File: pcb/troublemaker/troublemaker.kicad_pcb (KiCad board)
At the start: 2 copper layers, 419 x 394 mm, 116 parts, among them IC1 TEENSY_4.1, J1 neopixel_data_RPI19_GPIO10, J2 taptempo_led_RPI16_GPIO23, J3 5V_RPI2_OR_4, J4 GND_RPI34, J5 Conn_01x12, SW1 sw_eq2, SW10 sw_grain_playback, SW11 btn_sampler_stop, SW2 sw_eq1, SW3 sw_sub, SW4 sw_bass, SW5 sw_mid, SW6 sw_high, SW7 btn_delay_taptempo, SW8 sw_delay_type, SW9 sw_grain_type, U1 RASPBERRY_PI_4B_4GB, U2 CD74HC4067M, U3 CD74HC4067M, U4 CD74HC4067M, U5 CD74HC4067M, U6 CD74HC4067M

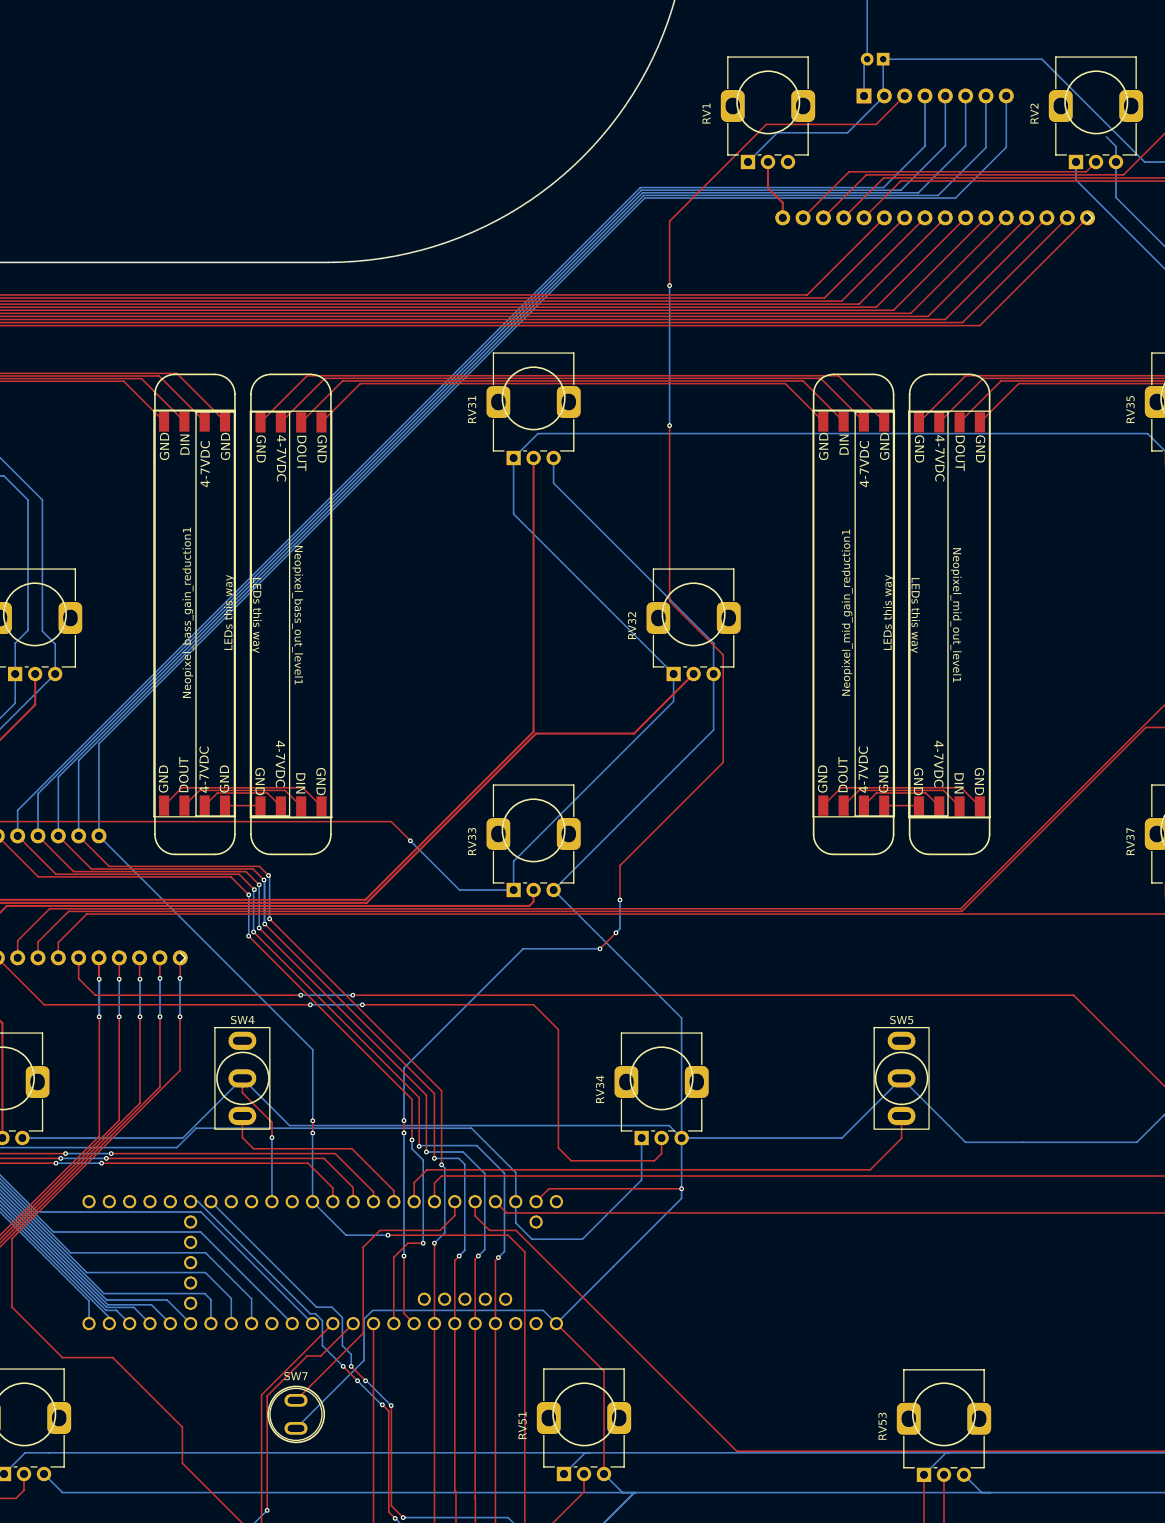
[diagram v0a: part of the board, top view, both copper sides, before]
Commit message: fixed missing connections
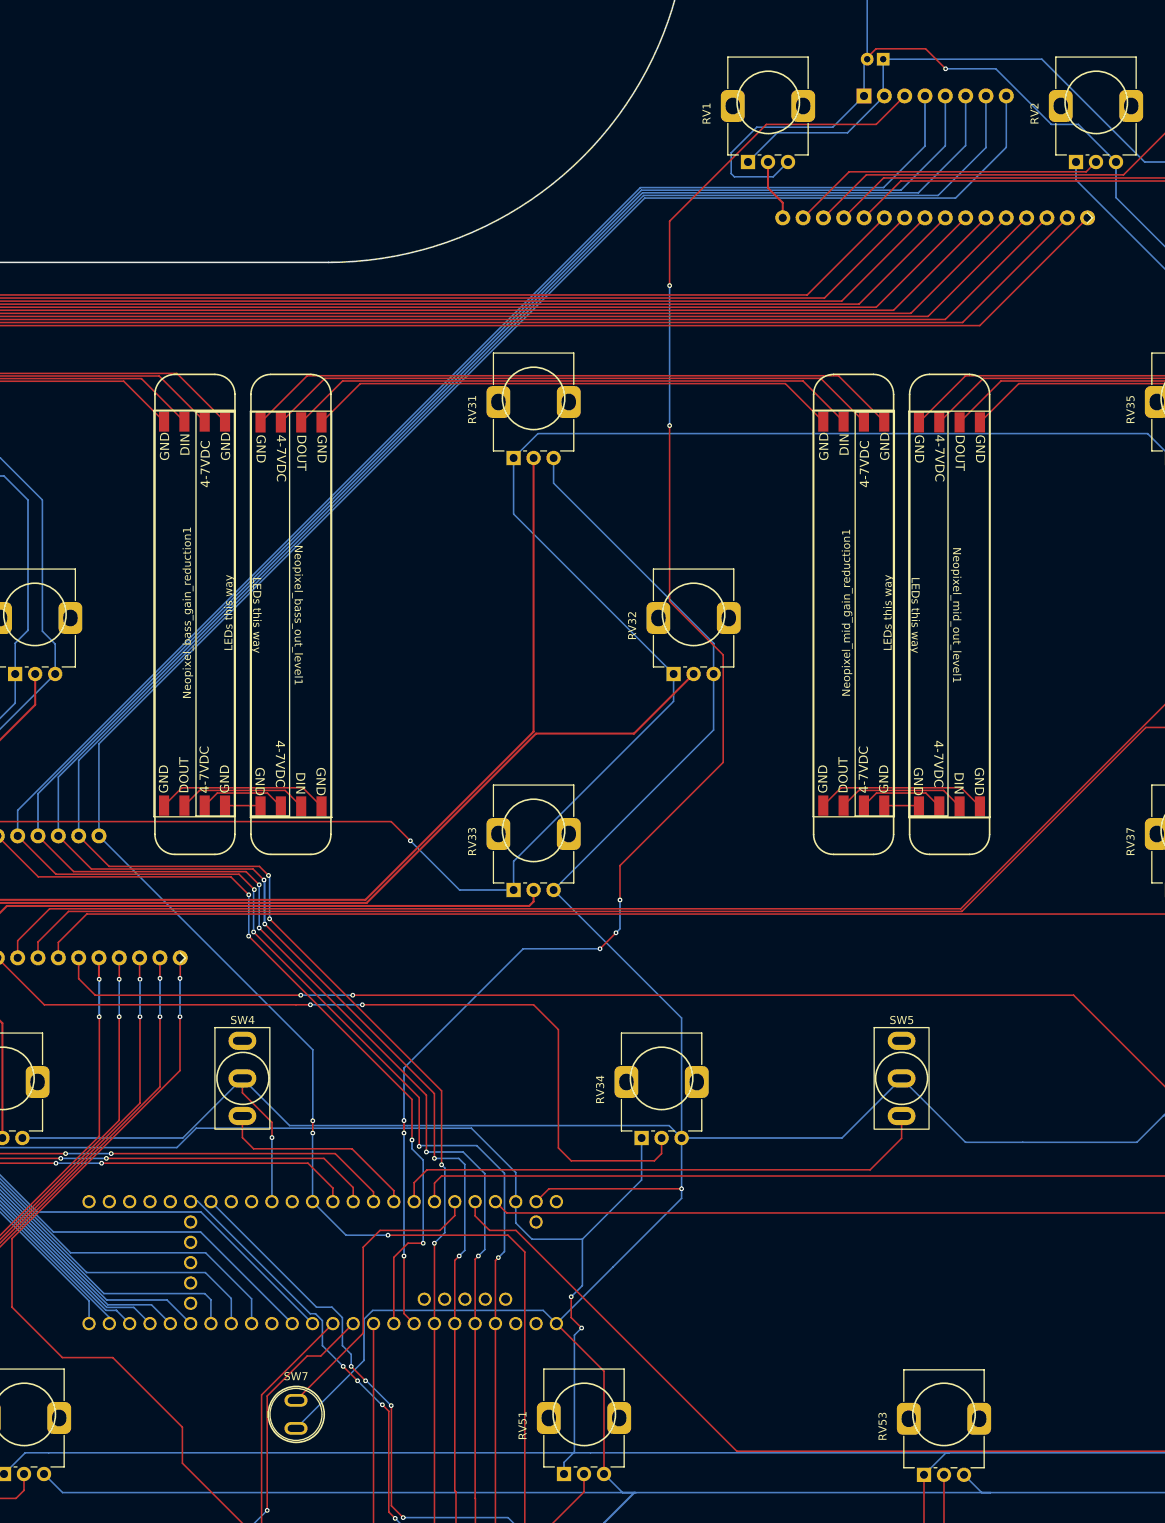
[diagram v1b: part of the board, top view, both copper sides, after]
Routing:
- net GND: track 3801.1 -> 3865.3 mm, vias 6 -> 7
- net 3v3: track 3703.4 -> 3730.4 mm, vias 8 -> 10
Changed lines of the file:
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@@
 	)
 	(segment
+		(start 314.9 209.6)
+		(end 316.2 210.9)
+		(width 0.2)
+		(layer "F.Cu")
+		(net 1)
+	)
+	(segment
 		(start 292.4 147.6)
 		(end 294.8 150)
@@
 	)
 	(segment
+		(start 314.9 207)
+		(end 314.9 209.6)
+		(width 0.2)
+		(layer "F.Cu")
+		(net 1)
+	)
+	(segment
 		(start 101.7304 216.15)
 		(end 102.5 216.15)
@@
 	)
 	(via
+		(at 314.9 207)
+		(size 0.6)
+		(drill 0.3)
+		(layers "F.Cu" "B.Cu")
+		(net 1)
+	)
+	(via
 		(at 390 78)
 		(size 0.6)
@@
 	)
 	(via
+		(at 316.2 210.9)
+		(size 0.6)
+		(drill 0.3)
+		(layers "F.Cu" "B.Cu")
+		(net 1)
+	)
+	(via
 		(at 235.6 153.3)
 		(size 0.6)
@@
 	)
 	(segment
-		(start 316.65 226.5)
-		(end 314 229.15)
-		(width 0.2)
-		(layer "B.Cu")
-		(net 1)
-	)
-	(segment
 		(start 292.1 255.3)
 		(end 292.1 259.535)
@@
 	)
 	(segment
+		(start 315.3 211.8)
+		(end 315.3 226.4)
+		(width 0.2)
+		(layer "B.Cu")
+		(net 1)
+	)
+	(segment
 		(start 372 297.15)
 		(end 388.8 313.95)
@@
 	)
 	(segment
+		(start 315.2 226.5)
+		(end 249.6 226.5)
+		(width 0.2)
+		(layer "B.Cu")
+		(net 1)
+	)
+	(segment
 		(start 292.45 259.885)
 		(end 295.715 263.15)
@@
 	)
 	(segment
+		(start 317.3 226.5)
+		(end 315.2 226.5)
+		(width 0.2)
+		(layer "B.Cu")
+		(net 1)
+	)
+	(segment
 		(start 437 34.25)
 		(end 438.2 33.05)
@@
 	)
 	(segment
-		(start 317.3 226.5)
-		(end 316.65 226.5)
-		(width 0.2)
-		(layer "B.Cu")
-		(net 1)
-	)
-	(segment
 		(start 44 156.15)
 		(end 44 206.65)
@@
 	)
 	(segment
+		(start 314 229.15)
+		(end 314 227.7)
+		(width 0.2)
+		(layer "B.Cu")
+		(net 1)
+	)
+	(segment
 		(start 256.7 348)
 		(end 256.85 348)
@@
 	)
 	(segment
+		(start 315.3 226.4)
+		(end 315.2 226.5)
+		(width 0.2)
+		(layer "B.Cu")
+		(net 1)
+	)
+	(segment
 		(start 367 348.7)
 		(end 366.1 347.8)
@@
 	)
 	(segment
+		(start 316.2 210.9)
+		(end 315.3 211.8)
+		(width 0.2)
+		(layer "B.Cu")
+		(net 1)
+	)
+	(segment
 		(start 334.2 347.8)
 		(end 335 348.6)
@@
 	)
 	(segment
+		(start 316.3 199.8)
+		(end 316.3 205.6)
+		(width 0.2)
+		(layer "B.Cu")
+		(net 1)
+	)
+	(segment
 		(start 247 107.4)
 		(end 247 123.7)
@@
 	)
 	(segment
+		(start 316.3 205.6)
+		(end 314.9 207)
+		(width 0.2)
+		(layer "B.Cu")
+		(net 1)
+	)
+	(segment
 		(start 64 128.15)
 		(end 51.55 128.15)
@@
 	)
 	(segment
-		(start 105.565074 139.1)
-		(end 109.8 139.1)
+		(start 314 227.7)
+		(end 315.2 226.5)
 		(width 0.2)
 		(layer "B.Cu")
@@
 	)
 	(segment
-		(start 53.5 319.15)
-		(end 53.5 285.15)
+		(start 105.565074 139.1)
+		(end 109.8 139.1)
 		(width 0.2)
 		(layer "B.Cu")
@@
 	)
 	(segment
-		(start 317.3 226.5)
-		(end 249.6 226.5)
+		(start 53.5 319.15)
+		(end 53.5 285.15)
 		(width 0.2)
 		(layer "B.Cu")
@@
 	)
 	(segment
+		(start 361.7 53.5)
+		(end 359.2 51)
+		(width 0.2)
+		(layer "F.Cu")
+		(net 2)
+	)
+	(segment
 		(start 146.125 219.675)
 		(end 146.7 219.1)
@@
 	)
 	(segment
+		(start 353 51)
+		(end 351.9 52.1)
+		(width 0.2)
+		(layer "F.Cu")
+		(net 2)
+	)
+	(segment
 		(start 184.2 89.4)
 		(end 190.7 89.4)
@@
 	)
 	(segment
+		(start 359.2 51)
+		(end 353 51)
+		(width 0.2)
+		(layer "F.Cu")
+		(net 2)
+	)
+	(segment
+		(start 351.9 52.1)
+		(end 351.9 52.3)
+		(width 0.2)
+		(layer "F.Cu")
+		(net 2)
+	)
+	(segment
 		(start 189.33 90.77)
 		(end 190.7 89.4)
@@
 	)
 	(via
+		(at 361.7 53.5)
+		(size 0.6)
+		(drill 0.3)
+		(layers "F.Cu" "B.Cu")
+		(net 2)
+	)
+	(via
 		(at 58.5 349)
 		(size 0.6)
@@
 	)
 	(segment
+		(start 338.1 60.8)
+		(end 347.595113 60.8)
+		(width 0.2)
+		(layer "B.Cu")
+		(net 2)
+	)
+	(segment
 		(start 58.5 285.15)
 		(end 58.5 319.15)
@@
 	)
 	(segment
+		(start 361.7 53.5)
+		(end 367.965074 53.5)
+		(width 0.2)
+		(layer "B.Cu")
+		(net 2)
+	)
+	(segment
 		(start 328.7 194.7)
 		(end 328.7 193.5)
@@
 	)
 	(segment
-		(start 381.8 62)
-		(end 383 63.2)
+		(start 279.7 185.6)
+		(end 294.410977 185.6)
 		(width 0.2)
 		(layer "B.Cu")
@@
 	)
 	(segment
-		(start 279.7 185.6)
-		(end 294.410977 185.6)
+		(start 58.5 349)
+		(end 58.5 326.5)
 		(width 0.2)
 		(layer "B.Cu")
@@
 	)
 	(segment
-		(start 58.5 349)
-		(end 58.5 326.5)
+		(start 378.3 60.45)
+		(end 383 65.15)
 		(width 0.2)
 		(layer "B.Cu")
@@
 	)
 	(segment
+		(start 374.915074 60.45)
+		(end 378.3 60.45)
+		(width 0.2)
+		(layer "B.Cu")
+		(net 2)
+	)
+	(segment
 		(start 107.5 216.15)
 		(end 107.5 251.15)
@@
 	)
 	(segment
+		(start 334.9 64)
+		(end 338.1 60.8)
+		(width 0.2)
+		(layer "B.Cu")
+		(net 2)
+	)
+	(segment
 		(start 88.3 319.7)
 		(end 90.3 321.7)
@@
 	)
 	(segment
+		(start 347.595113 60.8)
+		(end 351.505113 56.89)
+		(width 0.2)
+		(layer "B.Cu")
+		(net 2)
+	)
+	(segment
 		(start 334.2 294.8)
 		(end 374.65 294.8)
@@
 	)
 	(segment
+		(start 340.15 67)
+		(end 335.3 67)
+		(width 0.2)
+		(layer "B.Cu")
+		(net 2)
+	)
+	(segment
 		(start 58.5 326.5)
 		(end 63.3 321.7)
@@
 	)
 	(segment
-		(start 383 63.2)
-		(end 383 65.15)
-		(width 0.2)
-		(layer "B.Cu")
-		(net 2)
-	)
-	(segment
 		(start 139.5 389.1)
 		(end 139.85 389.1)
@@
 	)
 	(segment
+		(start 335.3 67)
+		(end 334.9 66.6)
+		(width 0.2)
+		(layer "B.Cu")
+		(net 2)
+	)
+	(segment
 		(start 441.05 263.15)
 		(end 443.5 260.7)
@@
 	)
 	(segment
+		(start 367.965074 53.5)
+		(end 374.915074 60.45)
+		(width 0.2)
+		(layer "B.Cu")
+		(net 2)
+	)
+	(segment
 		(start 90.24 288.92)
 		(end 88.3 290.86)
@@
 	)
 	(segment
+		(start 334.9 66.6)
+		(end 334.9 64)
+		(width 0.2)
+		(layer "B.Cu")
+		(net 2)
+	)
+	(segment
 		(start 443.5 260.7)
 		(end 443.5 260.3)
@@
 		(width 0.2)
 		(layer "B.Cu")
+		(net 2)
+	)
+	(segment
+		(start 342 65.15)
+		(end 340.15 67)
+		(width 0.2)
+		(layer "B.Cu")

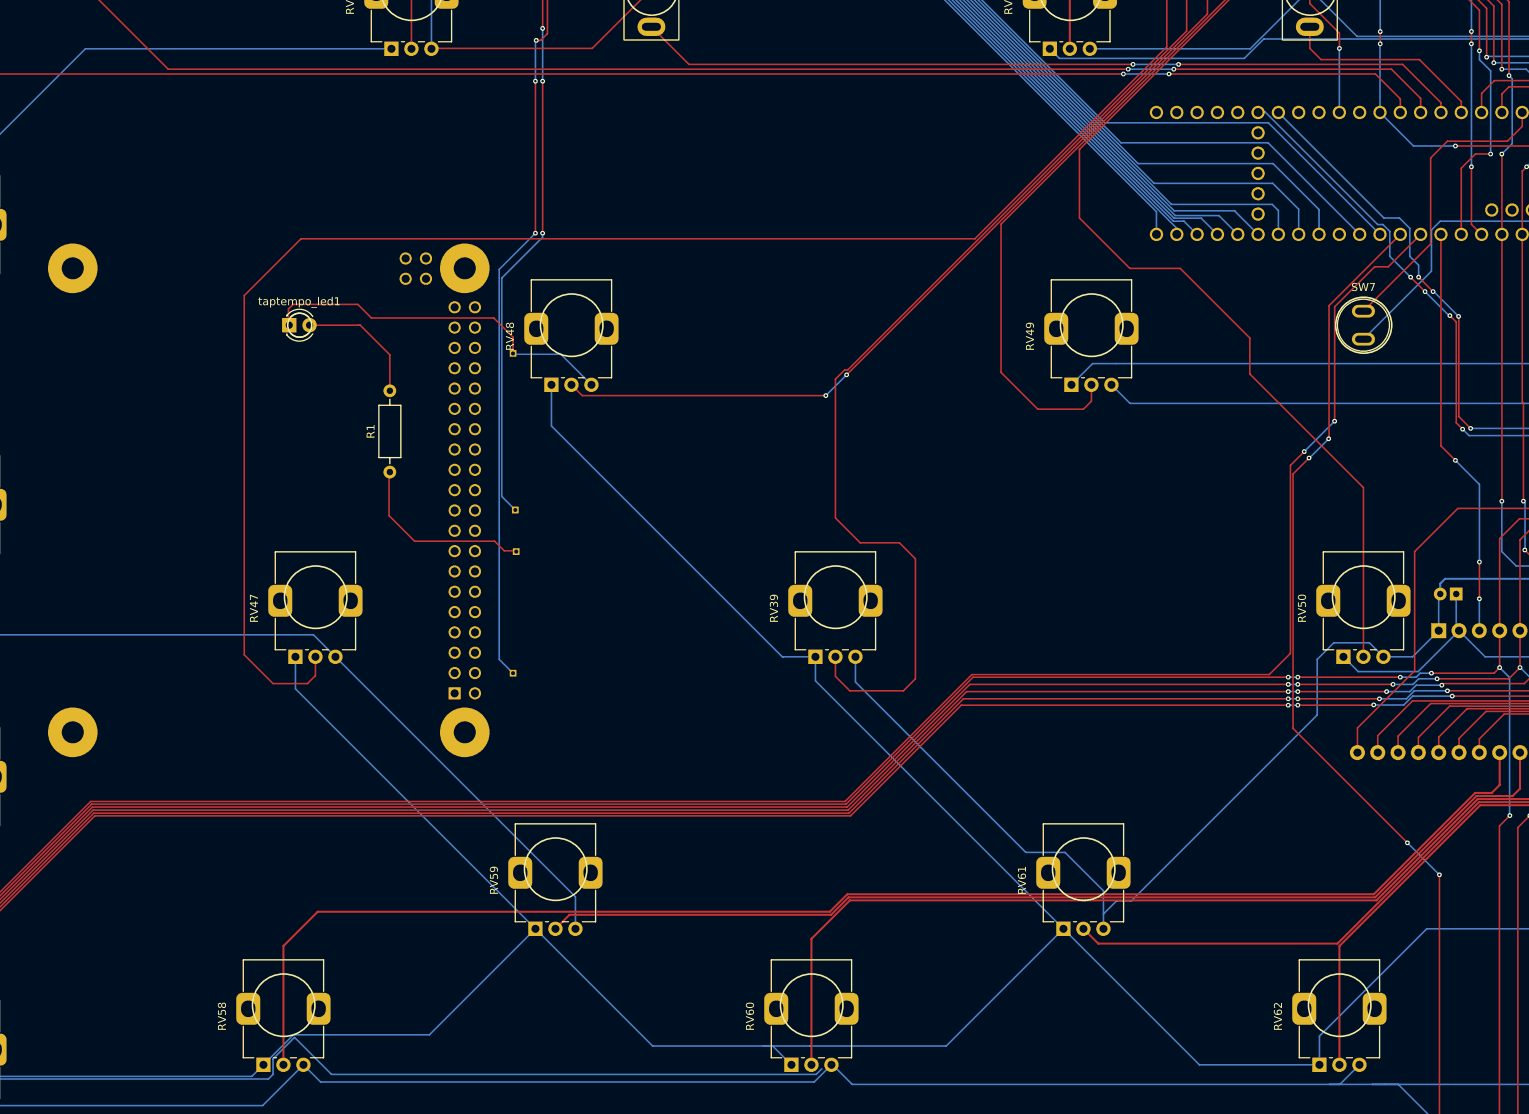
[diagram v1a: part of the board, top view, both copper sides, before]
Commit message: Removed pads from RPI footprint, added some text to jumpers
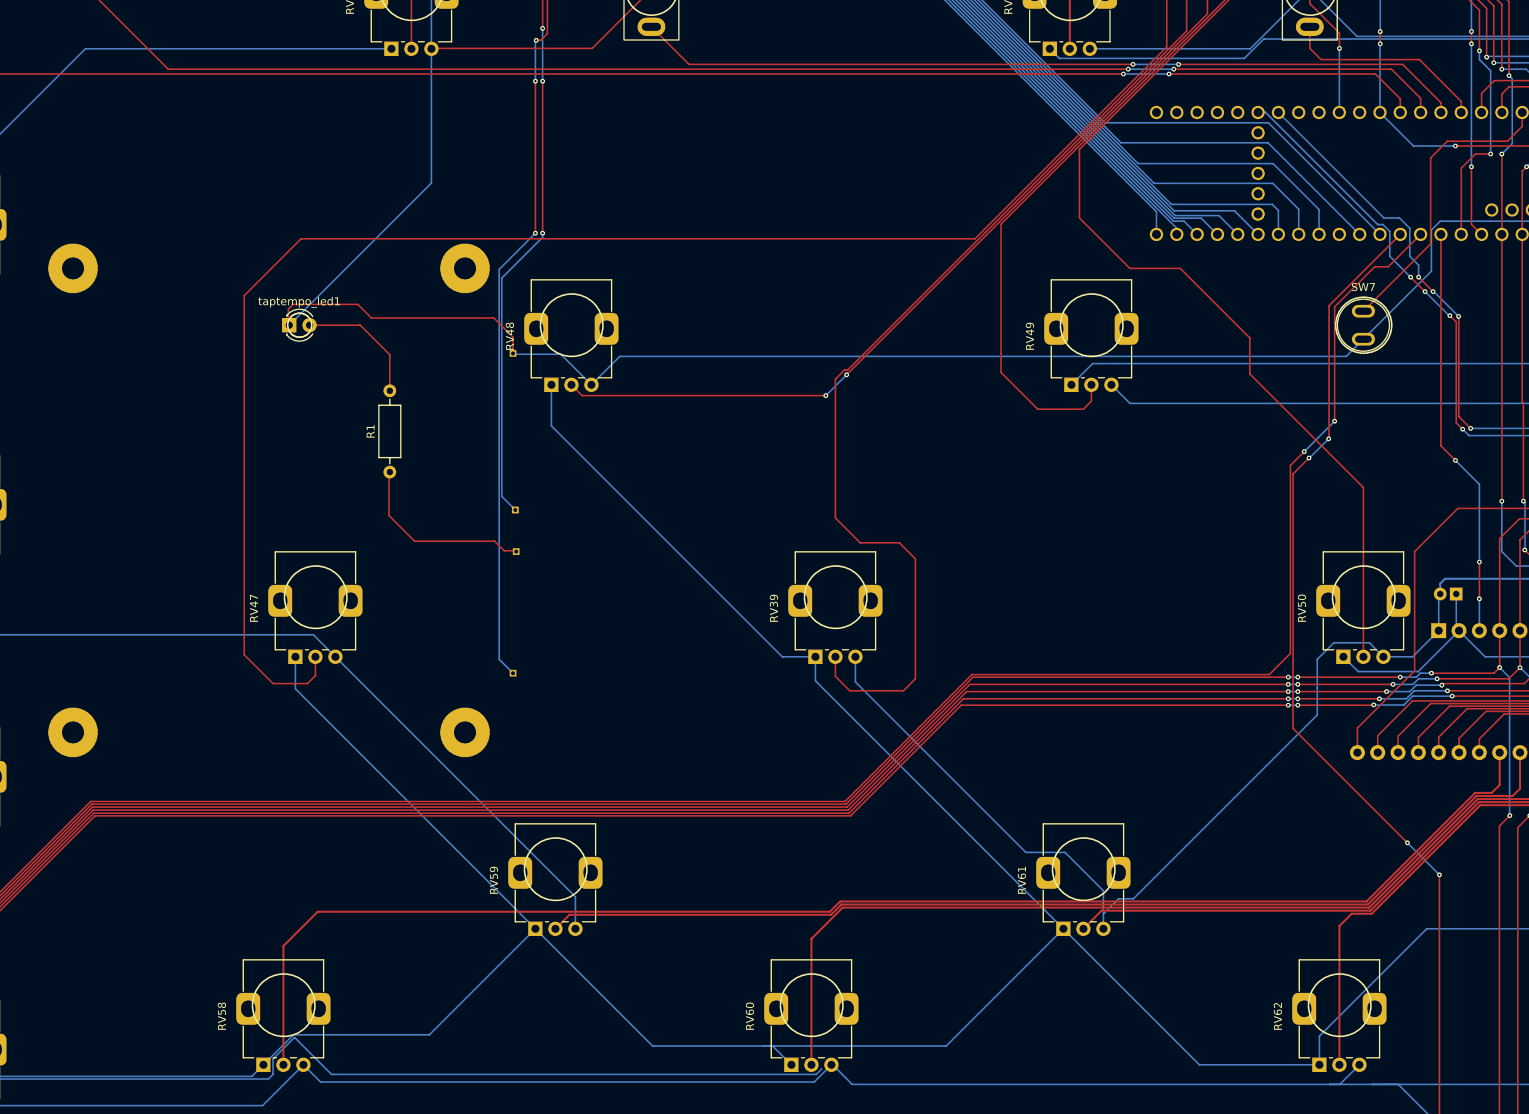
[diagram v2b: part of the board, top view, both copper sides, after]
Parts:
- removed U1: RASPBERRY_PI_4B_4GB, RASPBERRY_PI_4B_4GB:MODULE_RASPBERRY_PI_4B_4GB
- added RASPBERRY PI 4: RASPBERRY_PI_4B_4GB, Library:MODULE_RASPBERRY_PI_4B_4GB, B.Cu at (143.7, 233.6)
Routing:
- net GND: track 3865.3 -> 4006.0 mm
- net Net-(U4-I10): track 73.1 -> 71.6 mm
- net Net-(U4-I11): track 56.7 -> 58.1 mm
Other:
- board text added: "+5V PIN 2 OR 4"
- board text added: "GND"
- board text added: "NEOPIXEL DATA PIN19 GPIO10"
- board text added: "TAPTEMPO LED PIN16 GPIO23"
- board text added: "s1"
- board text added: "s10"
- board text added: "s11"
- board text added: "s2"
- board text added: "s3"
- board text added: "s4"
- board text added: "s5"
- board text added: "s6"
- board text added: "s7"
- board text added: "s8"
- board text added: "s9"

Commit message: Removed capacitors as I already have them on the breakout board. Small reroutes.
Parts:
- removed C1, C2, C3, C4, C5: C_Small, Capacitor_THT:CP_Radial_D5.0mm_P2.00mm
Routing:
- net GND: track 4006.0 -> 4254.6 mm, vias 7 -> 8
- net mux_s0: track 778.0 -> 631.6 mm
- net 3v3: track 3730.4 -> 3717.7 mm, vias 10 -> 8
- net Net-(U2-I9): track 288.5 -> 296.4 mm
- net Net-(U2-I6): track 331.5 -> 336.8 mm
- net Net-(U2-I14): track 315.0 -> 312.3 mm
- net mux4_enable: track 256.0 -> 257.5 mm
- net mux_s1: track 627.1 -> 627.9 mm
- net Net-(U3-I12): vias 2 -> 1
- net Net-(U3-I11): vias 2 -> 1
- net Net-(U3-I15): vias 2 -> 1
- net Net-(U3-I14): vias 2 -> 1
- net Net-(U3-I13): vias 4 -> 3
